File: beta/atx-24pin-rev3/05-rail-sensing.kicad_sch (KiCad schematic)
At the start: 29 parts, among them U10 INA238, U11 INA238, U12 INA238, U13 INA238, U612V1 INA181A2IDBVR, U63V31 INA181A2IDBVR, U65V1 INA181A2IDBVR, U65VSB1 INA181A2IDBVR, U712V1 TLV7011DBVR, U73V31 TLV7011DBVR, U75V1 TLV7011DBVR, U75VSB1 TLV7011DBVR

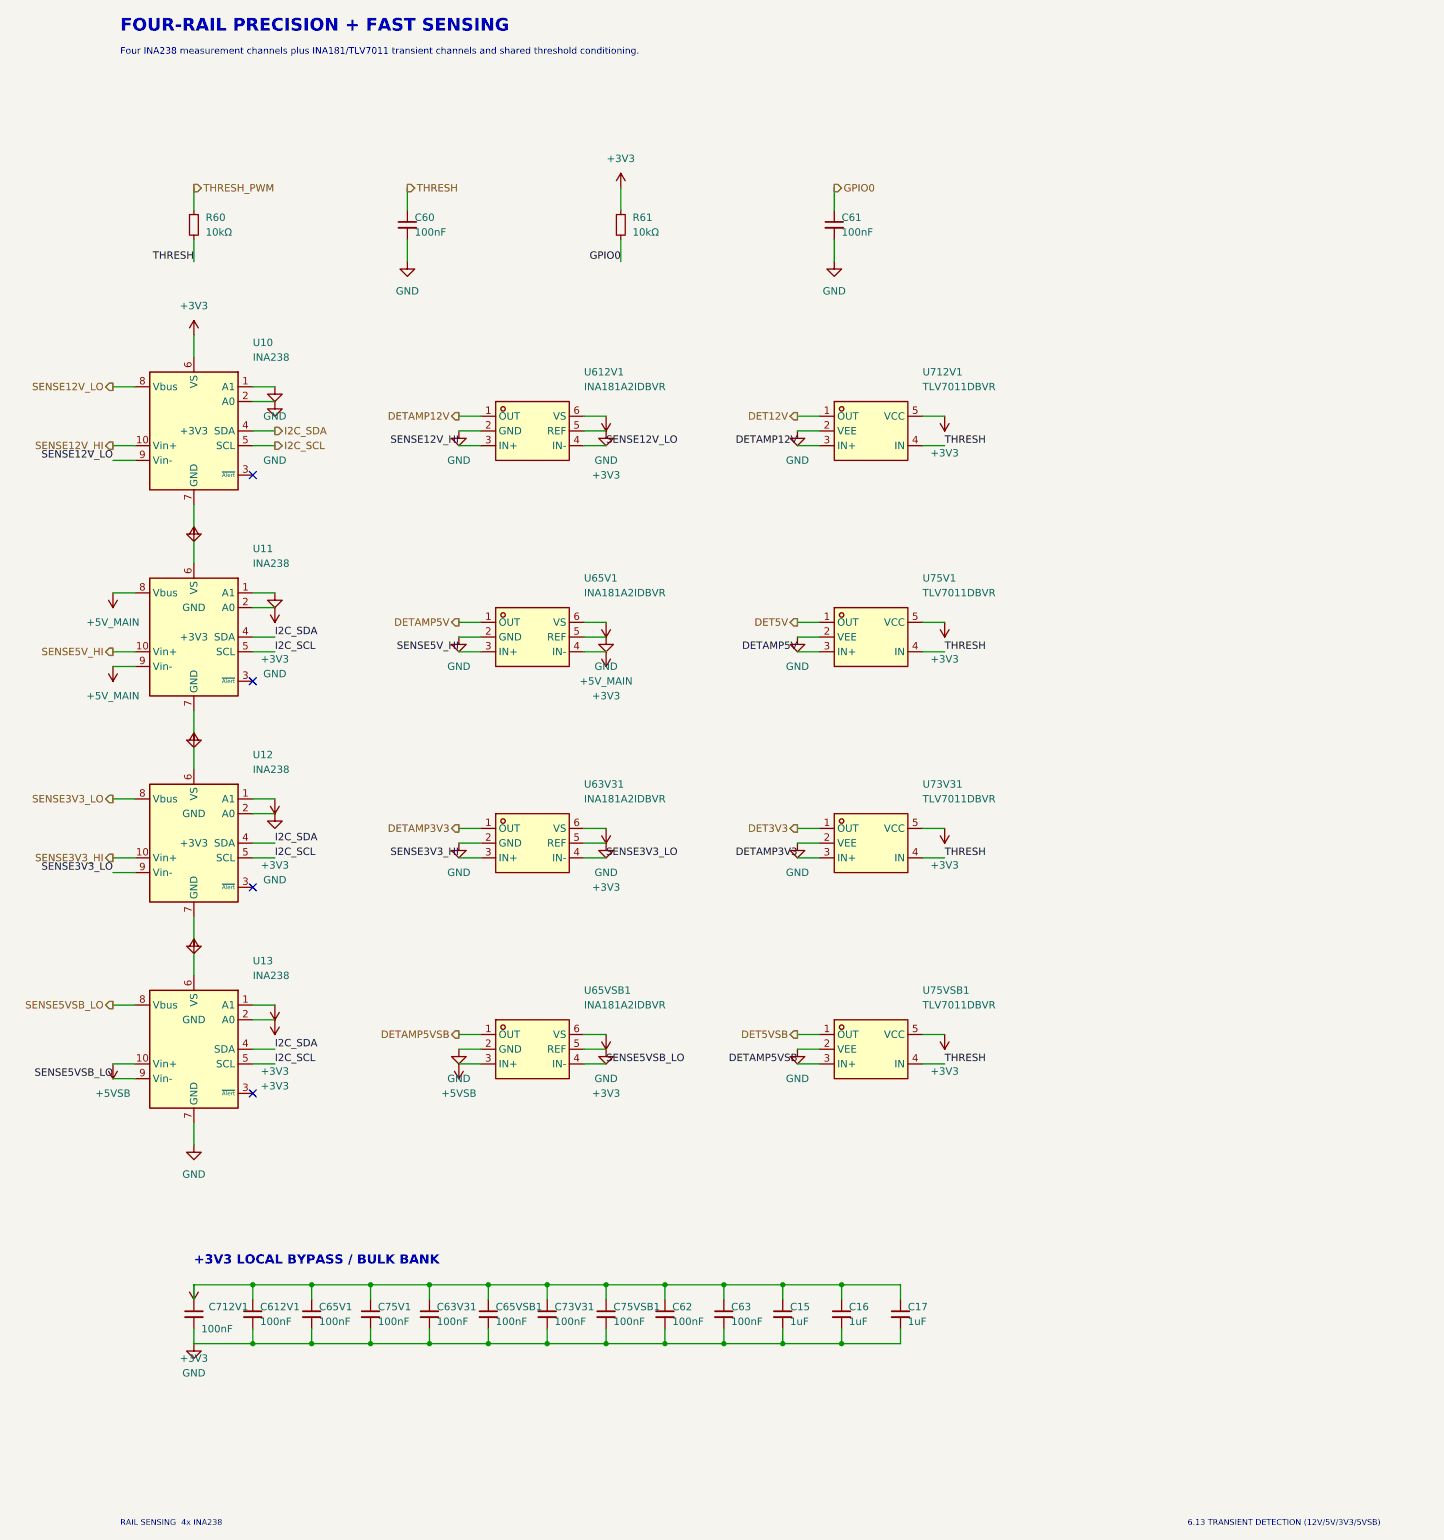
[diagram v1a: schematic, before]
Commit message: Finalize compact Hub and ATX power-layout audit
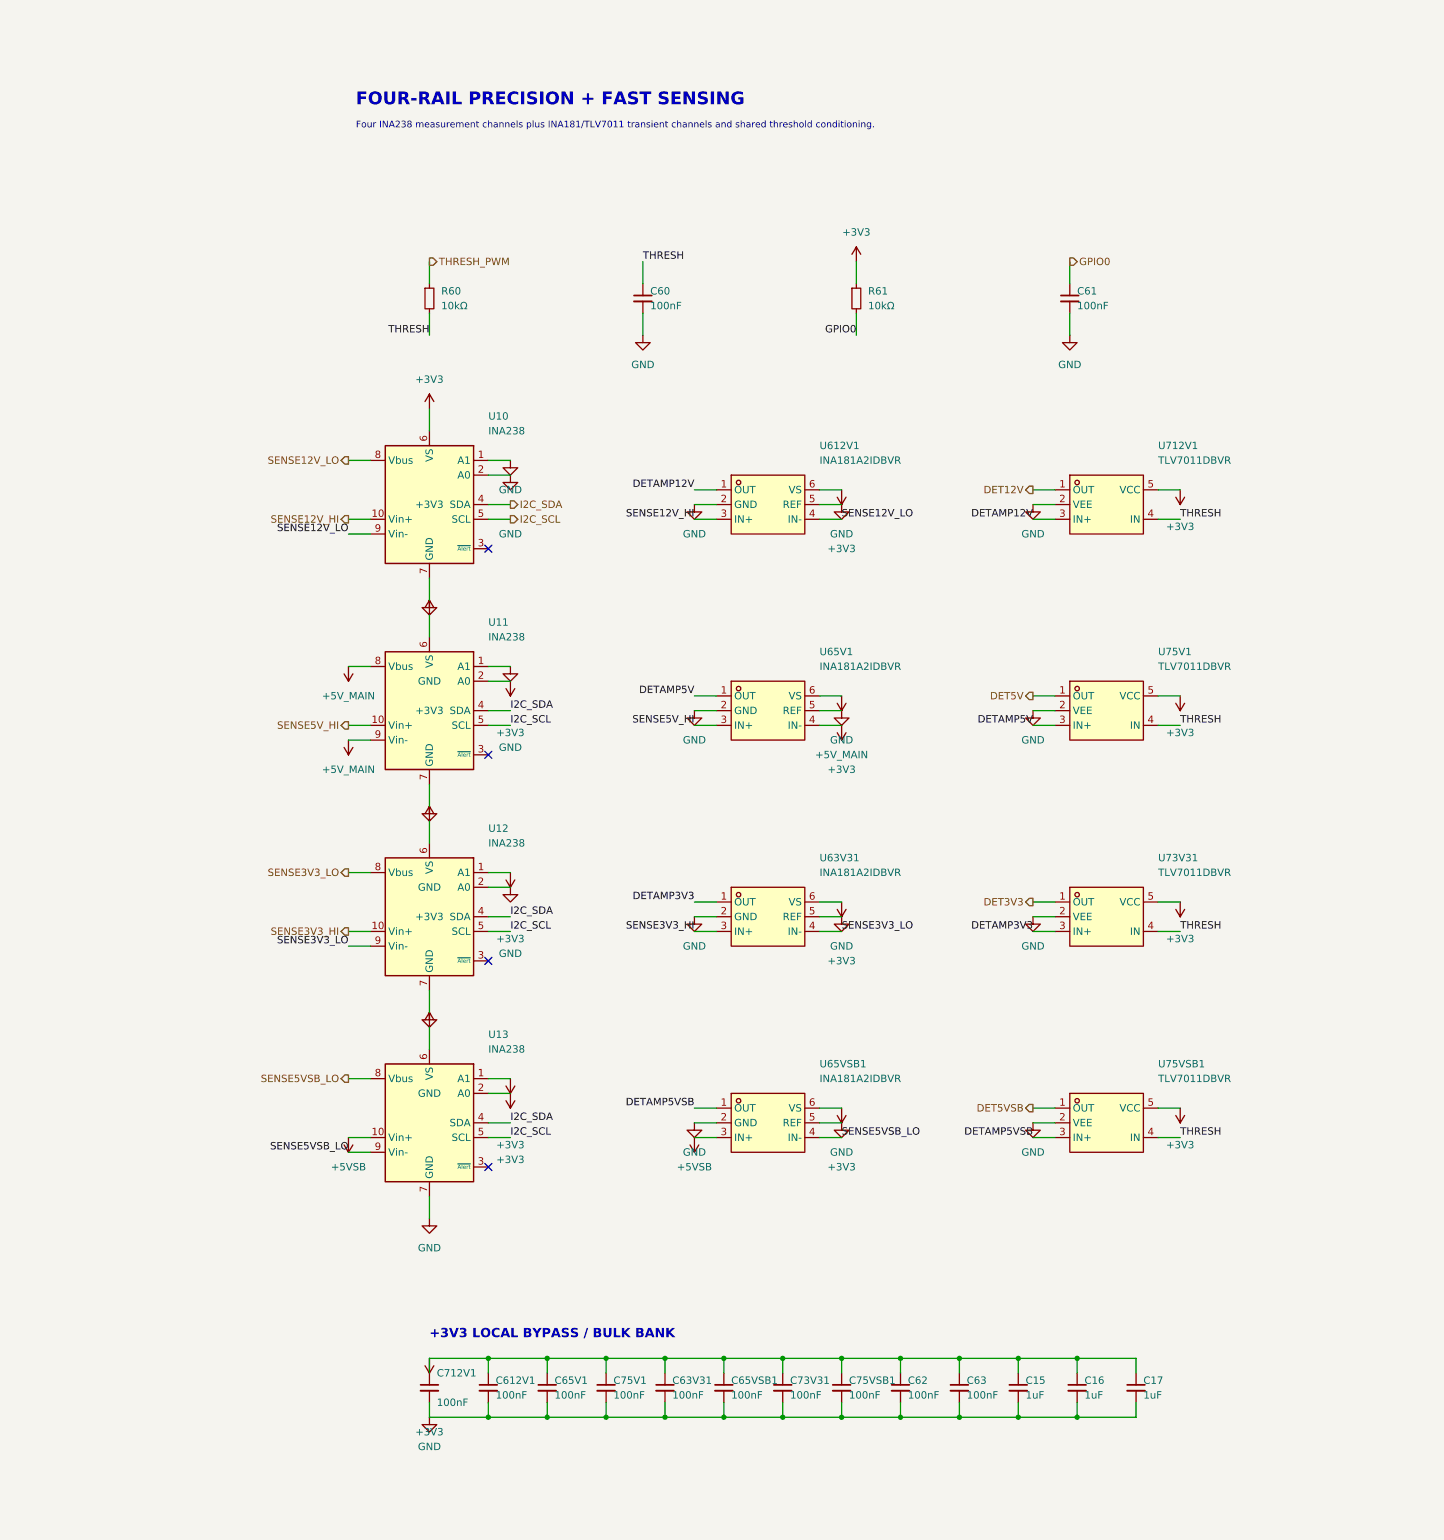
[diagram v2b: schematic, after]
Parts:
- C15: LCSC (none) -> C29936; MPN (none) -> CL10B105KA8NNNC; Manufacturer (none) -> Samsung; Note margin: INA238 U11 VS local bulk (place adjacent) -> Exact 1uF 25V X7R 0603 local bypass capacitor.
- C16: LCSC (none) -> C29936; MPN (none) -> CL10B105KA8NNNC; Manufacturer (none) -> Samsung; Note margin: INA238 U12 VS local bulk (place adjacent) -> Exact 1uF 25V X7R 0603 local bypass capacitor.
- C17: LCSC (none) -> C29936; MPN (none) -> CL10B105KA8NNNC; Manufacturer (none) -> Samsung; Note margin: INA238 U13 VS local bulk (place adjacent) -> Exact 1uF 25V X7R 0603 local bypass capacitor.
- R60, R61: LCSC (none) -> C25744; MPN (none) -> 0402WGF1002TCE; Manufacturer (none) -> UNI-ROYAL
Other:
- note removed: "6.13 TRANSIENT DETECTION (12V/5V/3V3/5VSB)"
- note removed: "RAIL SENSING 4x INA238"
